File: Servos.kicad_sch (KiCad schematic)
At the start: 1 part, among them J8 ${FAMILY}

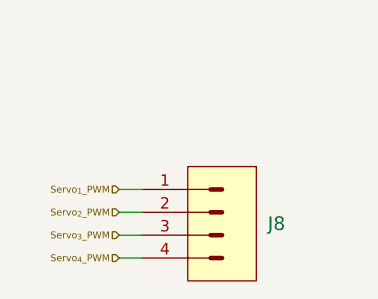
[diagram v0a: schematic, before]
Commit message: Changed some of the silkscreen, and added some LEDs attached to some gpio
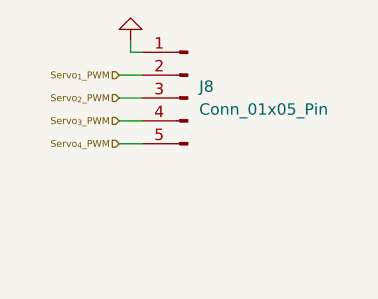
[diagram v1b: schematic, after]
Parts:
- removed J8: ${FAMILY}, SAMTEC THD:SAMTEC_BBL-104-X-E, symbol CERN:SAMTEC/SAMTEC_BBL-104-G-E
- added J8: Conn_01x05_Pin, Connector_PinHeader_2.54mm:PinHeader_1x05_P2.54mm_Vertical, symbol Connector:Conn_01x05_Pin
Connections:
- net Servo_{1}_PWM: now also J8.2 (Pin_2)
- net Servo_{2}_PWM: now also J8.3 (Pin_3)
- net Servo_{3}_PWM: now also J8.4 (Pin_4)
- net Servo_{4}_PWM: now also J8.5 (Pin_5)
- new net GND: J8.1 (Pin_1)
